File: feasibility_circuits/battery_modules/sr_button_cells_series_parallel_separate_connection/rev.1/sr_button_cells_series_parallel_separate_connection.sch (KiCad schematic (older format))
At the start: 25 parts

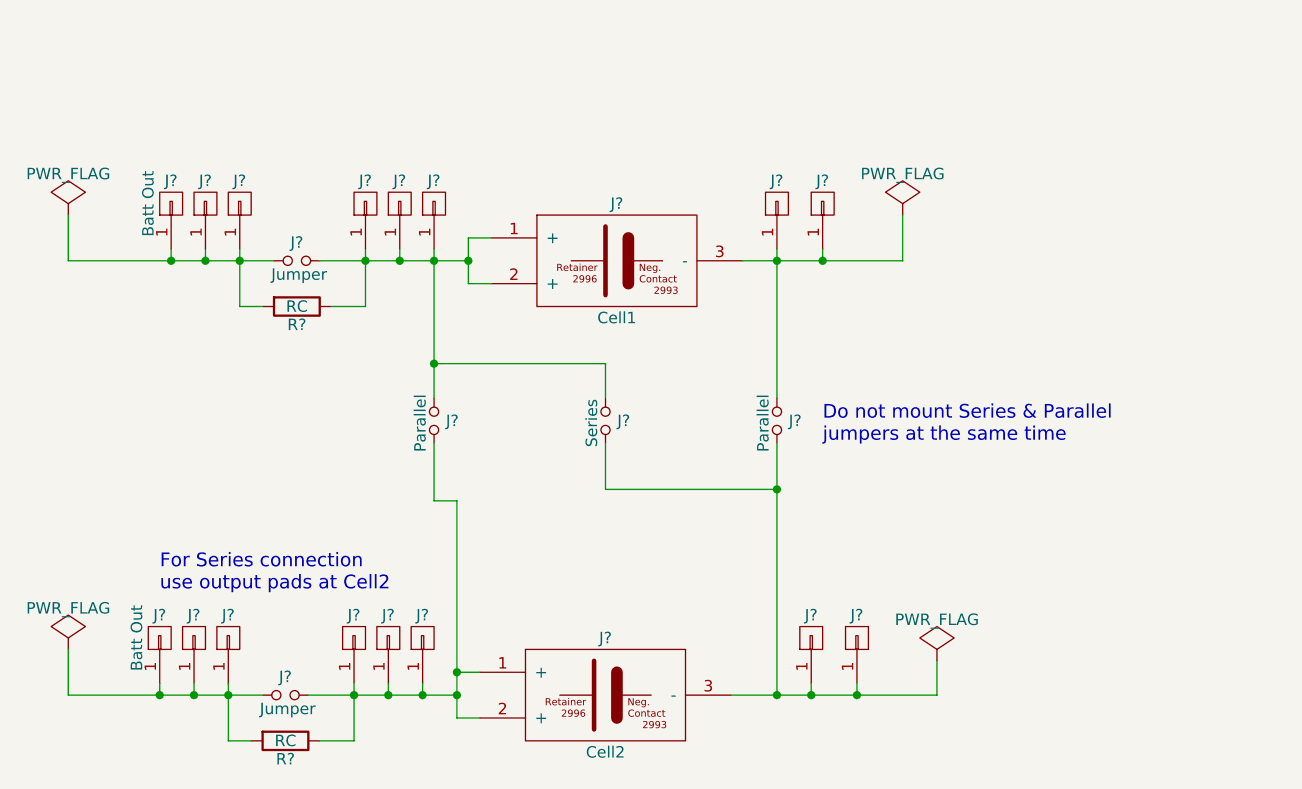
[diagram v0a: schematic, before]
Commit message: Completed initial draft of layout of battery board
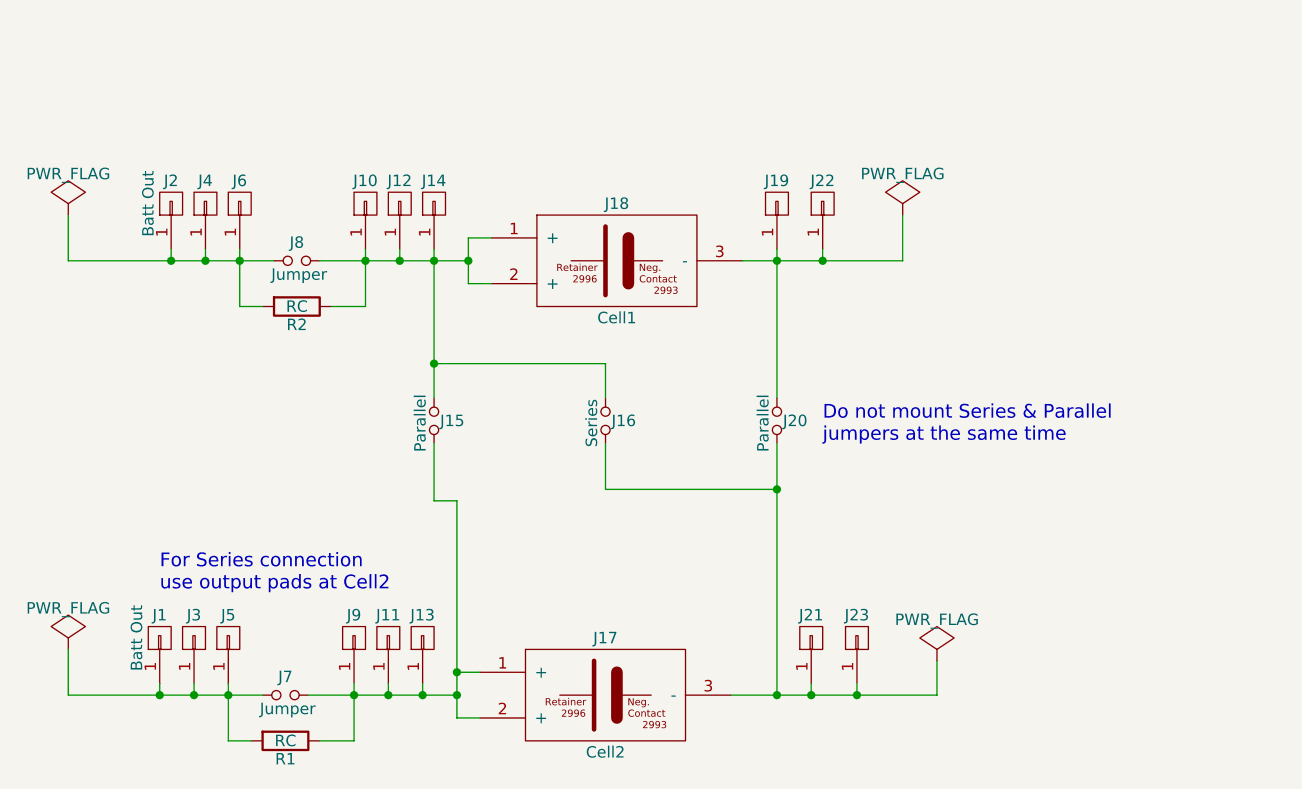
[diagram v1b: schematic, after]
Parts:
- J1, J10, J11, J12, J13, J14, J19, J2, J21, J22, J23, J3, J4, J5, J6, J9: renamed from J?; footprint (none) -> Custom Connectors:proto_pad-square-3mm
- J15, J16, J20, J7, J8: renamed from J?; footprint (none) -> Custom Connectors:proto_header-vt-1x2-2.54mm-G_C__SABN_M30
- J17, J18: renamed from J?; footprint (none) -> Custom Battery Products:proto_button_cell_holder-smd-2996-2993
- R1, R2: renamed from R?; footprint (none) -> Resistors_SMD:R_0805_HandSoldering

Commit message: Added files forgotten in last commit.
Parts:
- added J24: Lithium-Ion Cell, Custom Battery Products:proto_button_cell_holder-smd-498, symbol BUTTON_CELL_HOLDER/SMD/11.6MM/498
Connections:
- net at J10.1 (P1), J12.1 (P1), J14.1 (P1)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: now also J24.1 (+)
- net at J18.3 (-), J19.1 (P1), J20.1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: now also J24.2 (-)
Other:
- moved on the sheet: J16, J17, J18, J19, J20, J21, J22, J23
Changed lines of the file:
@@
 L BUTTON_CELL_HOLDER/SMD/11.6MM/2996/2993 J18
 U 1 1 5902EBB9
-P 6300 2500
-F 0 "J18" H 6300 2750 50  0000 C CNN
-F 1 "Cell1" H 6300 2250 50  0000 C CNN
-F 2 "Custom Battery Products:proto_button_cell_holder-smd-2996-2993" H 6300 2500 60  0001 C CNN
-F 3 "" H 6300 2500 60  0001 C CNN
-	1    6300 2500
+P 6450 2500
+F 0 "J18" H 6450 2750 50  0000 C CNN
+F 1 "Cell1" H 6450 2250 50  0000 C CNN
+F 2 "Custom Battery Products:proto_button_cell_holder-smd-2996-2993" H 6450 2500 60  0001 C CNN
+F 3 "" H 6450 2500 60  0001 C CNN
+	1    6450 2500
 	1    0    0    -1
 $EndComp
@@
 L CONN_01X01 J19
 U 1 1 5902F107
-P 7000 2250
-F 0 "J19" V 7100 2250 50  0000 C CNN
-F 1 "CONN_01X01" V 7100 2250 50  0001 C CNN
-F 2 "Custom Connectors:proto_pad-square-3mm" H 7000 2250 50  0001 C CNN
-F 3 "" H 7000 2250 50  0000 C CNN
-	1    7000 2250
+P 7250 2250
+F 0 "J19" V 7350 2250 50  0000 C CNN
+F 1 "CONN_01X01" V 7350 2250 50  0001 C CNN
+F 2 "Custom Connectors:proto_pad-square-3mm" H 7250 2250 50  0001 C CNN
+F 3 "" H 7250 2250 50  0000 C CNN
+	1    7250 2250
 	0    -1   -1   0
 $EndComp
@@
 L CONN_01X01 J22
 U 1 1 5902F168
-P 7200 2250
-F 0 "J22" V 7300 2250 50  0000 C CNN
-F 1 "CONN_01X01" V 7300 2250 50  0001 C CNN
-F 2 "Custom Connectors:proto_pad-square-3mm" H 7200 2250 50  0001 C CNN
-F 3 "" H 7200 2250 50  0000 C CNN
-	1    7200 2250
+P 7450 2250
+F 0 "J22" V 7550 2250 50  0000 C CNN
+F 1 "CONN_01X01" V 7550 2250 50  0001 C CNN
+F 2 "Custom Connectors:proto_pad-square-3mm" H 7450 2250 50  0001 C CNN
+F 3 "" H 7450 2250 50  0000 C CNN
+	1    7450 2250
 	0    -1   -1   0
 $EndComp
@@
 L BUTTON_CELL_HOLDER/SMD/11.6MM/2996/2993 J17
 U 1 1 5902F4E4
-P 6250 4400
-F 0 "J17" H 6250 4650 50  0000 C CNN
-F 1 "Cell2" H 6250 4150 50  0000 C CNN
-F 2 "Custom Battery Products:proto_button_cell_holder-smd-2996-2993" H 6250 4400 60  0001 C CNN
-F 3 "" H 6250 4400 60  0001 C CNN
-	1    6250 4400
+P 6400 4400
+F 0 "J17" H 6400 4650 50  0000 C CNN
+F 1 "Cell2" H 6400 4150 50  0000 C CNN
+F 2 "Custom Battery Products:proto_button_cell_holder-smd-2996-2993" H 6400 4400 60  0001 C CNN
+F 3 "" H 6400 4400 60  0001 C CNN
+	1    6400 4400
 	1    0    0    -1
 $EndComp
@@
 L CONN_01X01 J21
 U 1 1 5902F508
-P 7150 4150
-F 0 "J21" V 7250 4150 50  0000 C CNN
-F 1 "CONN_01X01" V 7250 4150 50  0001 C CNN
-F 2 "Custom Connectors:proto_pad-square-3mm" H 7150 4150 50  0001 C CNN
-F 3 "" H 7150 4150 50  0000 C CNN
-	1    7150 4150
+P 7400 4150
+F 0 "J21" V 7500 4150 50  0000 C CNN
+F 1 "CONN_01X01" V 7500 4150 50  0001 C CNN
+F 2 "Custom Connectors:proto_pad-square-3mm" H 7400 4150 50  0001 C CNN
+F 3 "" H 7400 4150 50  0000 C CNN
+	1    7400 4150
 	0    -1   -1   0
 $EndComp
@@
 L CONN_01X01 J23
 U 1 1 5902F50E
-P 7350 4150
-F 0 "J23" V 7450 4150 50  0000 C CNN
-F 1 "CONN_01X01" V 7450 4150 50  0001 C CNN
-F 2 "Custom Connectors:proto_pad-square-3mm" H 7350 4150 50  0001 C CNN
-F 3 "" H 7350 4150 50  0000 C CNN
-	1    7350 4150
+P 7600 4150
+F 0 "J23" V 7700 4150 50  0000 C CNN
+F 1 "CONN_01X01" V 7700 4150 50  0001 C CNN
+F 2 "Custom Connectors:proto_pad-square-3mm" H 7600 4150 50  0001 C CNN
+F 3 "" H 7600 4150 50  0000 C CNN
+	1    7600 4150
 	0    -1   -1   0
 $EndComp
@@
 L Jumper_NO_Small J20
 U 1 1 5902FD72
-P 7000 3200
-F 0 "J20" V 7000 3280 50  0000 C CNN
-F 1 "Parallel" H 7010 3140 50  0000 C CNN
-F 2 "Custom Connectors:proto_header-vt-1x2-2.54mm-G_C__SABN_M30" H 7000 3200 50  0001 C CNN
-F 3 "" H 7000 3200 50  0000 C CNN
-	1    7000 3200
+P 7250 3200
+F 0 "J20" V 7250 3280 50  0000 C CNN
+F 1 "Parallel" H 7260 3140 50  0000 C CNN
+F 2 "Custom Connectors:proto_header-vt-1x2-2.54mm-G_C__SABN_M30" H 7250 3200 50  0001 C CNN
+F 3 "" H 7250 3200 50  0000 C CNN
+	1    7250 3200
 	0    1    1    0
 $EndComp
@@
 L Jumper_NO_Small J16
 U 1 1 5902FDEA
-P 6250 3200
-F 0 "J16" V 6250 3280 50  0000 C CNN
-F 1 "Series" H 6260 3140 50  0000 C CNN
-F 2 "Custom Connectors:proto_header-vt-1x2-2.54mm-G_C__SABN_M30" H 6250 3200 50  0001 C CNN
-F 3 "" H 6250 3200 50  0000 C CNN
-	1    6250 3200
+P 6400 3200
+F 0 "J16" V 6400 3280 50  0000 C CNN
+F 1 "Series" H 6410 3140 50  0000 C CNN
+F 2 "Custom Connectors:proto_header-vt-1x2-2.54mm-G_C__SABN_M30" H 6400 3200 50  0001 C CNN
+F 3 "" H 6400 3200 50  0000 C CNN
+	1    6400 3200
 	0    1    1    0
 $EndComp
-Text Notes 7200 3300 0    60   ~ 0
+Text Notes 7450 3300 0    60   ~ 0
 Do not mount Series & Parallel\njumpers at the same time
 Text Notes 4300 3950 0    60   ~ 0
 For Series connection\nuse output pads at Cell2
 Wire Wire Line
-	5750 2400 5650 2400
-Wire Wire Line
-	5650 2400 5650 2600
-Wire Wire Line
-	5650 2600 5750 2600
-Connection ~ 5650 2500
+	5900 2400 5800 2400
+Wire Wire Line
+	5800 1800 5800 2600
+Wire Wire Line
+	5800 2600 5900 2600
+Connection ~ 5800 2500
 Connection ~ 5500 2500
 Wire Wire Line
@@
 	4650 2700 4750 2700
 Wire Wire Line
-	6850 2500 7550 2500
-Wire Wire Line
-	7000 2450 7000 3100
-Wire Wire Line
-	7200 2500 7200 2450
-Connection ~ 7000 2500
-Wire Wire Line
-	5700 4300 5600 4300
-Wire Wire Line
-	5600 4500 5700 4500
-Connection ~ 5600 4400
+	7250 2450 7250 3100
+Wire Wire Line
+	7450 2500 7450 2450
+Connection ~ 7250 2500
+Wire Wire Line
+	5850 4300 5750 4300
+Wire Wire Line
+	5750 4500 5850 4500
+Connection ~ 5750 4400
 Wire Wire Line
 	3900 4400 4750 4400
@@
 Wire Wire Line
 	4600 4600 4700 4600
-Connection ~ 5600 4300
-Wire Wire Line
-	5600 3550 5600 4500
+Connection ~ 5750 4300
+Wire Wire Line
+	5750 3550 5750 4500
 Wire Wire Line
 	5500 3300 5500 3550
 Wire Wire Line
-	5500 3550 5600 3550
+	5500 3550 5750 3550
 Wire Wire Line
 	5500 2450 5500 3100
 Wire Wire Line
-	7150 4350 7150 4400
-Wire Wire Line
-	6800 4400 7700 4400
-Wire Wire Line
-	7350 4400 7350 4350
-Connection ~ 7150 4400
-Wire Wire Line
-	7000 3300 7000 4400
-Connection ~ 7000 4400
-Wire Wire Line
-	6250 3100 6250 2950
-Wire Wire Line
-	6250 2950 5500 2950
+	7400 4350 7400 4400
+Wire Wire Line
+	7600 4400 7600 4350
+Connection ~ 7400 4400
+Wire Wire Line
+	7250 3300 7250 4400
+Connection ~ 7250 4400
+Wire Wire Line
+	6400 2950 6400 3100
+Wire Wire Line
+	5500 2950 6400 2950
 Connection ~ 5500 2950
 Wire Wire Line
-	6250 3300 6250 3500
-Wire Wire Line
-	6250 3500 7000 3500
-Connection ~ 7000 3500
+	6400 3300 6400 3500
+Connection ~ 7250 3500
 $Comp
 L CONN_01X01 J2
@@
 L PWR_FLAG #FLG02
 U 1 1 5903141A
-P 7550 2300
-F 0 "#FLG02" H 7550 2395 50  0001 C CNN
-F 1 "PWR_FLAG" H 7550 2480 50  0000 C CNN
-F 2 "" H 7550 2300 50  0000 C CNN
-F 3 "" H 7550 2300 50  0000 C CNN
-	1    7550 2300
-	1    0    0    -1
-$EndComp
-Wire Wire Line
-	7550 2500 7550 2300
-Connection ~ 7200 2500
+P 7800 2300
+F 0 "#FLG02" H 7800 2395 50  0001 C CNN
+F 1 "PWR_FLAG" H 7800 2480 50  0000 C CNN
+F 2 "" H 7800 2300 50  0000 C CNN
+F 3 "" H 7800 2300 50  0000 C CNN
+	1    7800 2300
+	1    0    0    -1
+$EndComp
+Wire Wire Line
+	7800 2500 7800 2300
+Connection ~ 7450 2500
 Wire Wire Line
 	3900 2300 3900 2500
@@
 L PWR_FLAG #FLG04
 U 1 1 590315C4
-P 7700 4250
-F 0 "#FLG04" H 7700 4345 50  0001 C CNN
-F 1 "PWR_FLAG" H 7700 4430 50  0000 C CNN
-F 2 "" H 7700 4250 50  0000 C CNN
-F 3 "" H 7700 4250 50  0000 C CNN
-	1    7700 4250
-	1    0    0    -1
-$EndComp
-Wire Wire Line
-	7700 4400 7700 4250
-Connection ~ 7350 4400
+P 7950 4250
+F 0 "#FLG04" H 7950 4345 50  0001 C CNN
+F 1 "PWR_FLAG" H 7950 4430 50  0000 C CNN
+F 2 "" H 7950 4250 50  0000 C CNN
+F 3 "" H 7950 4250 50  0000 C CNN
+	1    7950 4250
+	1    0    0    -1
+$EndComp
+Wire Wire Line
+	7950 4400 7950 4250
+Connection ~ 7600 4400
 $Comp
 L CONN_01X01 J10
@@
 	5200 2700 5200 2450
 Wire Wire Line
-	5000 2500 5650 2500
+	5000 2500 5800 2500
 Wire Wire Line
 	5050 2700 5200 2700
@@
 	5450 4350 5450 4400
 Wire Wire Line
-	4950 4400 5600 4400
+	4950 4400 5750 4400
 Wire Wire Line
 	5300 4350 5300 4400
@@
 Wire Wire Line
 	5150 4600 5000 4600
+$Comp
+L BUTTON_CELL_HOLDER/SMD/11.6MM/498 J24
+U 1 1 59045D1C
+P 6450 1800
+F 0 "J24" H 6450 1500 60  0000 C CNN
+F 1 "Lithium-Ion Cell" H 6450 2100 60  0000 C CNN
+F 2 "Custom Battery Products:proto_button_cell_holder-smd-498" H 6450 1800 60  0001 C CNN
+F 3 "" H 6450 1800 60  0001 C CNN
+	1    6450 1800
+	1    0    0    -1
+$EndComp
+Wire Wire Line
+	7000 2500 7800 2500
+Wire Wire Line
+	6400 3500 7250 3500
+Wire Wire Line
+	6950 4400 7950 4400
+Wire Wire Line
+	5800 1800 5900 1800
+Connection ~ 5800 2400
+Wire Wire Line
+	7000 1800 7050 1800
+Wire Wire Line
+	7050 1800 7050 2500
+Connection ~ 7050 2500
 $EndSCHEMATC
